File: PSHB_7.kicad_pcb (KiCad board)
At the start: 6 copper layers, 119.3 x 62.3 mm, 98 parts, among them J7 DS1013-20SSIB1-B-0, Q1 C3M0065100K, Q3 C3M0065100K

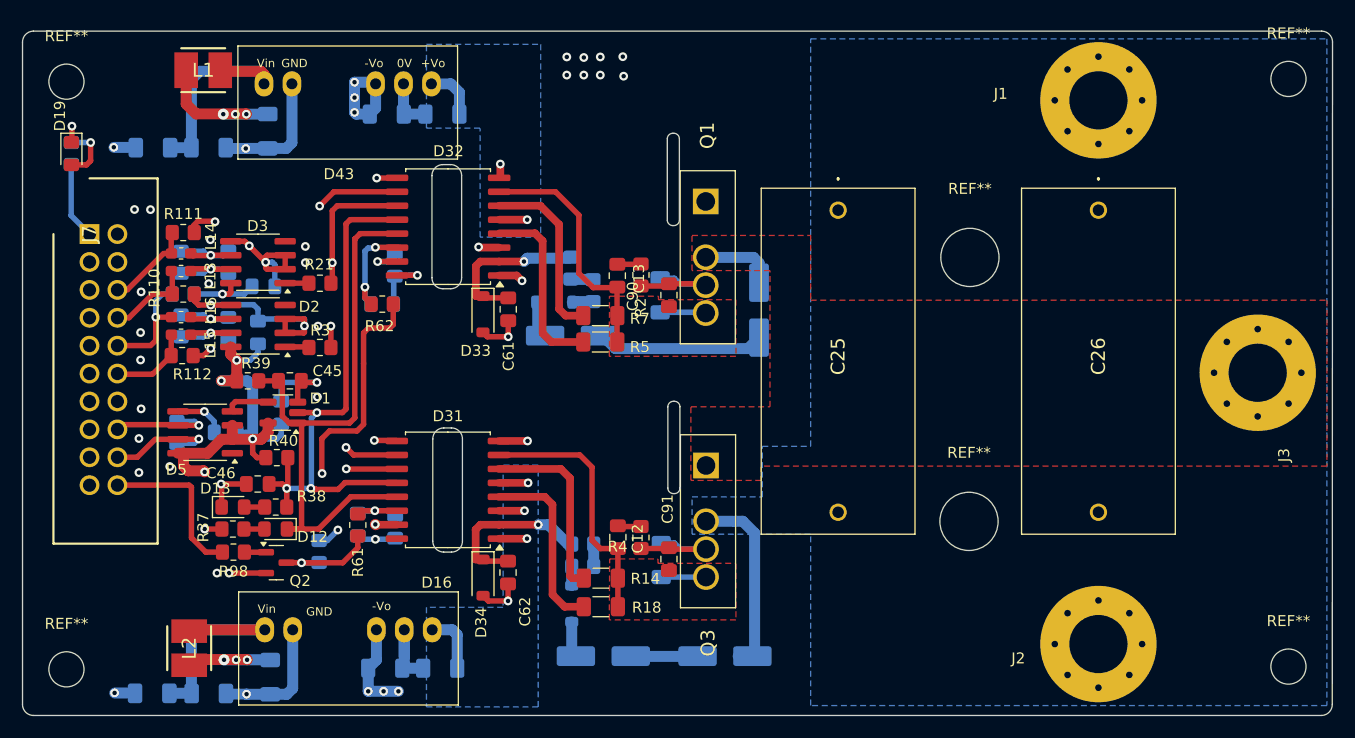
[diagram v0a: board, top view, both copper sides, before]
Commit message: Поменял десат подключение, сделал зазоры на силовых полигонах
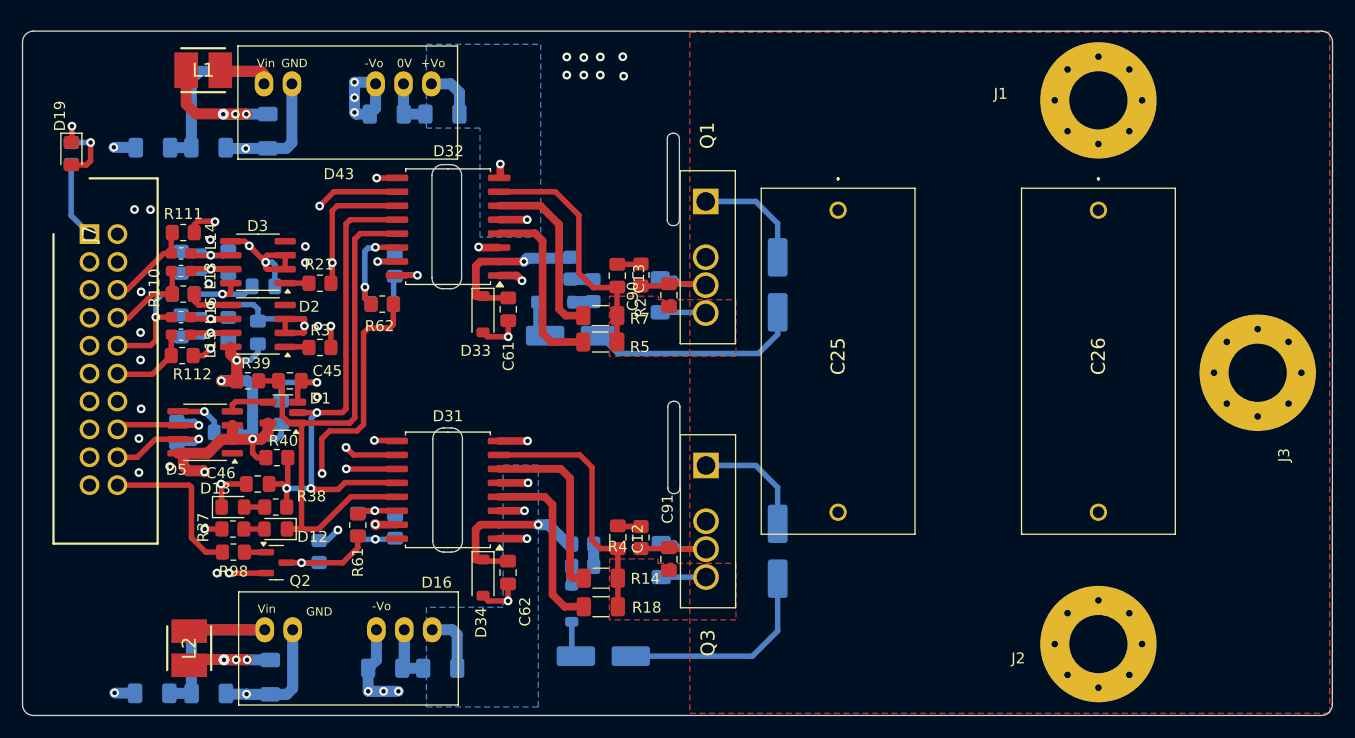
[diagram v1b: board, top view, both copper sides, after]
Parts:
- removed REF** (x4): MountingHole_3.2mm_M3, MountingHole:MountingHole_3.2mm_M3
- removed REF** (x2): MountingHole_5.3mm_M5, MountingHole:MountingHole_5.3mm_M5
- R67, R68: value 560 -> 220
- moved D6 10.7 mm to (427.0, 157.8), turned to -90 degrees
- moved D4 2.86 mm to (427.0, 133.5)
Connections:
- C10 pad 2: DS1 -> D2
- C14 pad 1: DS1 -> D2
- C25 pad 2: S2 -> DS2
- C26 pad 2: S2 -> DS2
- C61 pad 2: DS1 -> D2
- C90 pad 1: DS1 -> D2
- D32 pad 3: DS1 -> D2
- D33 pad 2: DS1 -> D2
- D4 pad 1: D2 -> D1
- D43 pad 6: DS1 -> D2
- D6 pad 1: S2 -> D2
- J2 pad 1: S2 -> DS2
- Q1 pad 3: DS1 -> D2
- Q3 pad 2: S2 -> DS2
- R104 pad 1: DS1 -> D2
- R2 pad 1: DS1 -> D2
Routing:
- net D2: track 6.86 -> 31.8 mm, vias 0 -> 10
- net DS1: track 21.2 -> 0.00 mm, vias 10 -> 0
- net S2: track 17.4 -> 0.00 mm
- net Net-(D59-K): track 5.99 -> 19.1 mm
- net D1: track 0.00 -> 10.5 mm
- net Net-(D4-A): track 15.0 -> 19.6 mm
- net Net-(D35-A): track 2.07 -> 3.39 mm
- net Net-(D36-A): track 2.67 -> 3.28 mm
- added copper zone on In4.Cu, net D1
- added copper zone on In3.Cu, net D2
- added copper zone on In4.Cu, net D2
- added copper zone on In2.Cu, net DS2
- removed copper zone on In1.Cu, net DS1
- removed copper zone on In3.Cu, net DS1
- removed copper zone on In4.Cu, net DS1
- removed copper zone on B.Cu, net S2
- removed copper zone on In4.Cu, net S2
